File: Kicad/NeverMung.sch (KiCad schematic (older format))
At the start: 13 parts

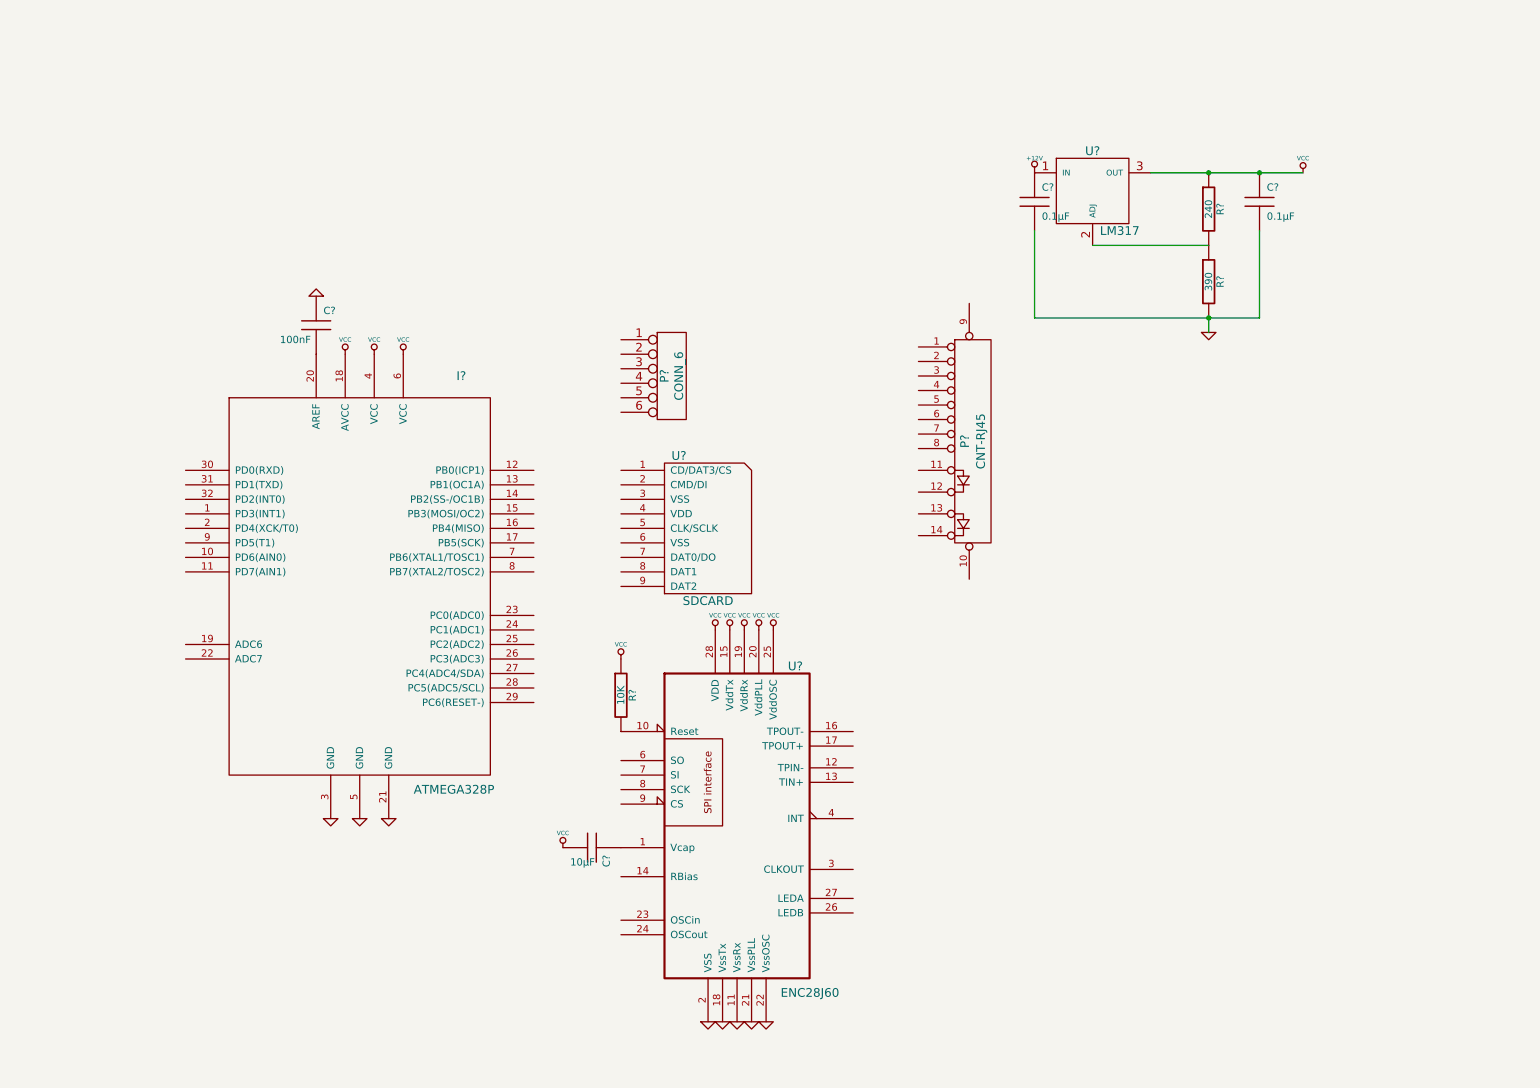
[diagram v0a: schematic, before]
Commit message: Started layout
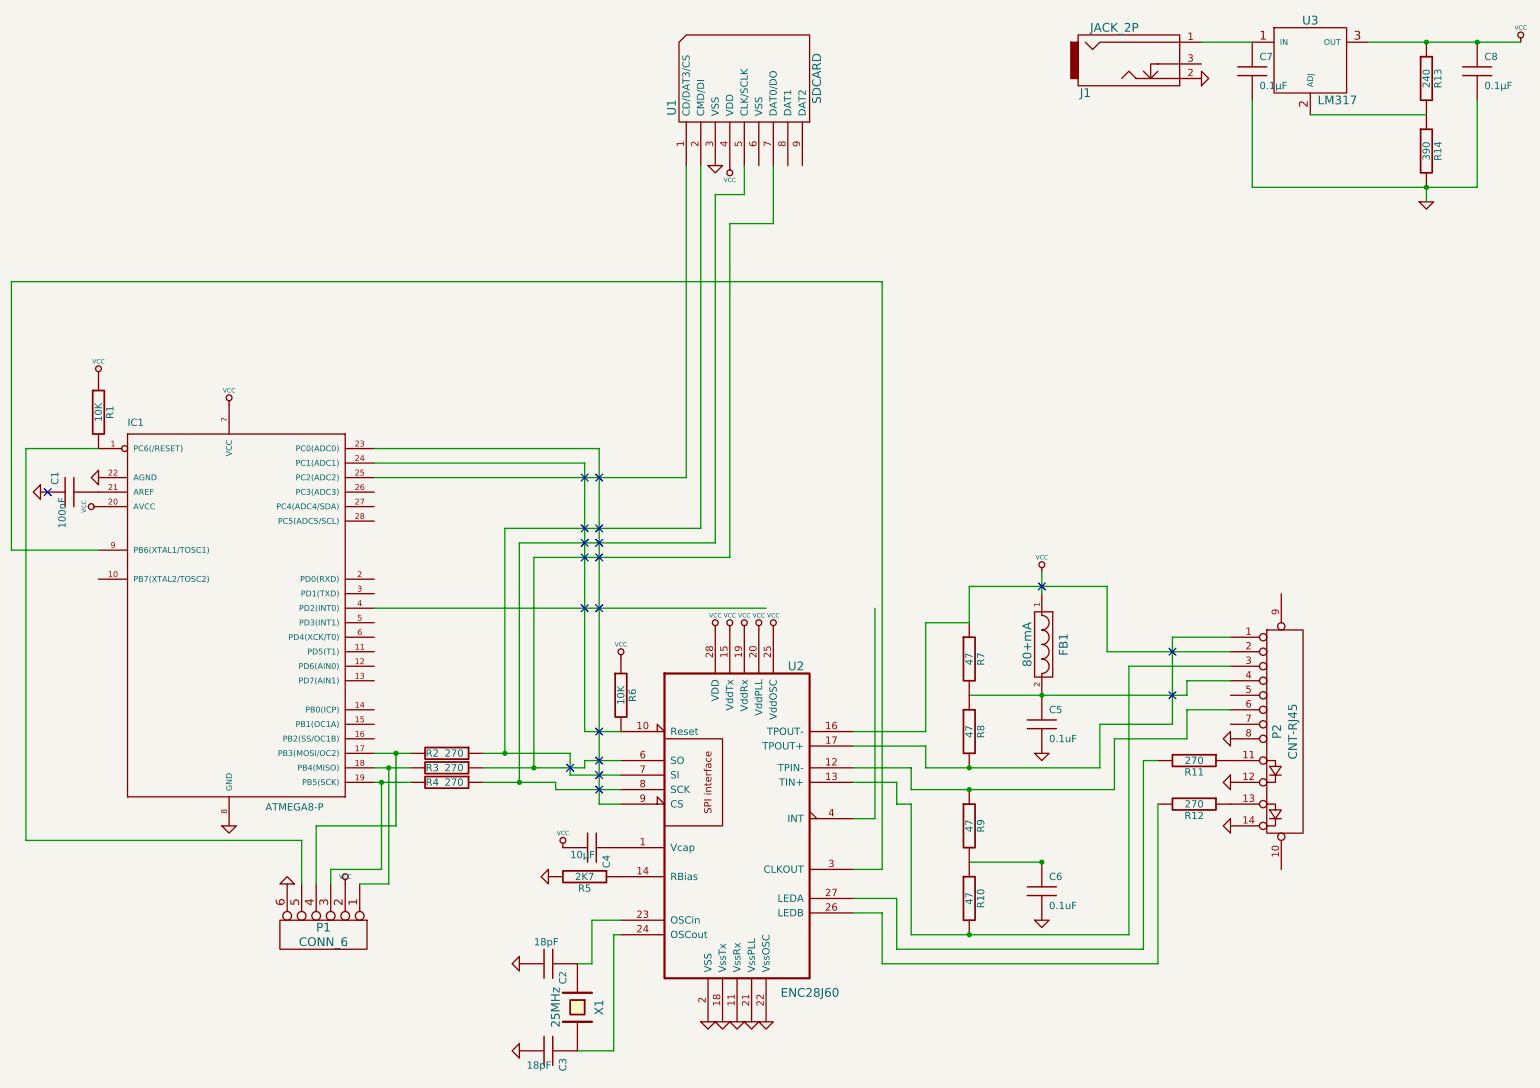
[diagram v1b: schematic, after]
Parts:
- removed I?: ATMEGA328P, symbol ATMEGA8
- added C2, C3: 18pF, symbol C
- added C5, C6: 0.1uF, symbol C
- added FB1: 80+mA, symbol FILTER
- added IC1: ATMEGA8-P, DIL28, symbol ATMEGA8-P
- added J1: JACK_2P, symbol JACK_2P
- added R1: 10K, symbol R
- added R10, R7, R8, R9: 47, symbol R
- added R11, R12, R2, R3, R4: 270, symbol R
- added R5: 2K7, symbol R
- added X1: 25MHz, symbol CRYSTAL
- gave numbers to parts that had none: 12
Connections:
- net GND: now also P1.6, P2.12 (P12), P2.14 (P14), P2.8 (P8), U1.3 (VSS), C2.2, C3.2, C5.2, C6.2, IC1.22 (AGND), IC1.8 (GND), J1.2, R5.2
- net VCC: now also P1.2, U1.4 (VDD), FB1.1, IC1.20 (AVCC), IC1.7 (VCC), R1.1
- net at C1.2: now also IC1.21 (AREF)
- net at U1.1 (CD/DAT3/CS): now also IC1.25 (PC2(ADC2))
- net at U1.2 (CMD/DI): now also U2.7 (SI), R2.1
- net at U1.5 (CLK/SCLK): now also U2.8 (SCK), R4.1
- net at U1.7 (DAT0/DO): now also U2.6 (SO), R3.1
- net at P1.1: now also IC1.18 (PB4(MISO)), R3.2
- net at P1.3: now also IC1.19 (PB5(SCK)), R4.2
- net at P1.4: now also IC1.17 (PB3(MOSI/OC2)), R2.2
- net at P1.5: now also IC1.1 (PC6(/RESET)), R1.2
- net at R6.2, U2.10 (Reset): now also IC1.24 (PC1(ADC1))
- net at U2.12 (TPIN-): now also P2.6 (P6), R9.1
- net at U2.13 (TIN+): now also P2.3 (P3), R10.2
- net at U2.14 (RBias): now also R5.1
- net at U2.16 (TPOUT-): now also P2.2 (P2), R7.1
- net at U2.17 (TPOUT+): now also P2.1 (P1), R8.2
- net at U2.23 (OSCin): now also C2.1, X1.1
- net at U2.24 (OSCout): now also C3.1, X1.2
- net at U2.26 (LEDB): now also R12.2
- net at U2.27 (LEDA): now also R11.2
- net at U2.3 (CLKOUT): now also IC1.9 (PB6(XTAL1/TOSC1))
- net at U2.9 (CS): now also IC1.23 (PC0(ADC0))
- net at P2.11 (P11): now also R11.1
- net at P2.13 (P13): now also R12.1
- net at P2.4 (P4): now also C5.1, FB1.2, R7.2, R8.1
- net +12V: no longer names the net of C7.1, U3.1 (IN)
- net +12V: now also J1.1
- new net: C6.1, R10.1, R9.2
- no-connect marks 0 -> 19
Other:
- moved on the sheet: C1, C7, C8, P1, P2, R13, R14, U1, U3
